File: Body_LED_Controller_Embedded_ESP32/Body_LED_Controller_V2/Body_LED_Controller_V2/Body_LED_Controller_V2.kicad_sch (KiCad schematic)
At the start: 94 parts, among them J1 SERIAL, J10 USB_B_Micro, J11 USB_B_Micro, J12 UnSW_BATT_IN, J13 Conn_02x03_Odd_Even, J14 DomeControllerUSB, J15 DomePlateControllerUSB, J16 UnSW_BATT_PASS, J17 RADH_POW, J18 RASP_POW, J19 5V_OUT_3, J2 I2C, J20 ICSP, J21 DomeElectronicsPowerIn, J22 DB25_Female_MountingHoles, J23 Amplifier_POW, J3 Conn_02x10_Odd_Even, J4 LDP/MAINT, J5 COIN/VU, J6 Batt Level LEDS, J7 Data Panel/ CBI, J8 Spectrum Analyzer, J9 Ext Mic, SW1 SW_Push, SW2 SW_Push, U1 ATMEGA256016AU, U14 D36V50F5-STEPDOWN, U2 CH340C, U3 CJ2301_S1, U4 ESP32-WROOM-32U_16MB_, U5 CH340C, U6 UMH3N, U7 ME6211C33M5G, U8 CJ2301_S1, Y1 16MHz

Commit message: Added a lot since last check in
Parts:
- removed D1, D2: SMD-LED-CLEAR-BLUE(0402), Custom:LED-0402, symbol Custom:SMD-LED-CLEAR-BLUE(0402)
- removed J1: SERIAL, Connector_PinHeader_2.54mm:PinHeader_2x04_P2.54mm_Vertical, symbol Connector_Generic:Conn_02x04_Odd_Even
- removed J13: Conn_02x03_Odd_Even, Connector_PinHeader_2.54mm:PinHeader_2x03_P2.54mm_Vertical, symbol Connector_Generic:Conn_02x03_Odd_Even
- removed J2: I2C, Connector_PinHeader_2.54mm:PinHeader_2x04_P2.54mm_Vertical, symbol Connector_Generic:Conn_02x04_Odd_Even
- removed J4: LDP/MAINT, Connector_PinHeader_2.54mm:PinHeader_2x04_P2.54mm_Vertical, symbol Connector_Generic:Conn_02x04_Odd_Even
- removed J5: COIN/VU, Connector_PinHeader_2.54mm:PinHeader_2x06_P2.54mm_Vertical, symbol Connector_Generic:Conn_02x06_Odd_Even
- removed J9: Ext Mic, Connector_PinHeader_2.54mm:PinHeader_1x03_P2.54mm_Vertical, symbol Connector_Generic:Conn_01x03
- removed R15, R16: 1K, Resistor_SMD:R_0402_1005Metric, symbol Device:R
- removed R4, R5: 10K, Resistor_SMD:R_0402_1005Metric, symbol Device:R
- added J1, J2: Body Servos, Connector_Molex:Molex_KK-254_AE-6410-03A_1x03_P2.54mm_Vertical, symbol Connector_Generic:Conn_01x03
- added J13: Batt Level LEDS, Connector_Molex:Molex_KK-254_AE-6410-04A_1x04_P2.54mm_Vertical, symbol Connector_Generic:Conn_01x04
- added J24: Future, Connector_Molex:Molex_KK-254_AE-6410-03A_1x03_P2.54mm_Vertical, symbol Connector_Generic:Conn_01x03
- added J25: Stealth, Connector_Molex:Molex_KK-254_AE-6410-03A_1x03_P2.54mm_Vertical, symbol Connector_Generic:Conn_01x03
- added J26: RADH, Connector_Molex:Molex_KK-254_AE-6410-03A_1x03_P2.54mm_Vertical, symbol Connector_Generic:Conn_01x03
- added J27: VU Data Panel, Connector_Molex:Molex_KK-254_AE-6410-06A_1x06_P2.54mm_Vertical, symbol Connector_Generic:Conn_01x06
- added J4: LDP, Connector_Molex:Molex_KK-254_AE-6410-04A_1x04_P2.54mm_Vertical, symbol Connector_Generic:Conn_01x04
- added J5: Coin Slots, Connector_Molex:Molex_KK-254_AE-6410-06A_1x06_P2.54mm_Vertical, symbol Connector_Generic:Conn_01x06
- added J9: Maintenance, Connector_Molex:Molex_KK-254_AE-6410-04A_1x04_P2.54mm_Vertical, symbol Connector_Generic:Conn_01x04
- J6: footprint Connector_PinHeader_2.54mm:PinHeader_1x04_P2.54mm_Vertical -> Connector_Molex:Molex_KK-254_AE-6410-04A_1x04_P2.54mm_Vertical
- J7: footprint Connector_PinHeader_2.54mm:PinHeader_1x05_P2.54mm_Vertical -> Connector_Molex:Molex_KK-254_AE-6410-05A_1x05_P2.54mm_Vertical
- J8: footprint Connector_PinHeader_2.54mm:PinHeader_1x06_P2.54mm_Vertical -> Connector_Molex:Molex_KK-254_AE-6410-06A_1x06_P2.54mm_Vertical
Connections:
- net +3.3V_BC: no longer L2.4 (VDD)
- net +5V: now also L2.4 (VDD), J1.2 (Pin_2), J13.2 (Pin_2), J27.2 (Pin_2), J4.2 (Pin_2), J5.2 (Pin_2), J9.2 (Pin_2)
- net CS1_CLOCK: now also J5.3 (Pin_3)
- net CS2_CLOCK: now also J5.5 (Pin_5)
- net EXT_MIC: now also J1.3 (Pin_3)
- net GND: now also J1.1 (Pin_1), J13.1 (Pin_1), J2.1 (Pin_1), J24.1 (Pin_1), J25.1 (Pin_1), J26.1 (Pin_1), J27.1 (Pin_1), J4.1 (Pin_1), J5.1 (Pin_1), J9.1 (Pin_1)
- net LDP_CLOCK: now also J4.3 (Pin_3)
- net MAINT_CLOCK: now also J9.3 (Pin_3)
- net RXD0_BC: now also U4.34 (RXD0)
- net RX_BL: now also U4.23 (IO15); no longer U4.11 (IO26)
- net RX_BS: now also U4.16 (IO13), J2.2 (Pin_2); no longer U4.27 (IO16)
- net RX_MP: now also U4.8 (IO32), J13.3 (Pin_3); no longer U4.28 (IO17)
- net RX_ST: now also U4.7 (IO35), J25.2 (Pin_2); no longer U4.14 (IO12)
- net ST_LED_D_BC: now also U4.29 (IO5); no longer U4.30 (IO18)
- net TX_BL: now also U4.27 (IO16); no longer U4.10 (IO25)
- net TX_BS: now also U4.13 (IO14), J2.3 (Pin_3); no longer U4.23 (IO15)
- net TX_MP: now also U4.30 (IO18), J13.4 (Pin_4); no longer U4.29 (IO5)
- net TX_ST: now also U4.31 (IO19), J25.3 (Pin_3); no longer U4.13 (IO14)
- net VU1_CLOCK: now also J27.3 (Pin_3)
- net VU2_CLOCK: now also J27.5 (Pin_5)
- net at R9.1: now also J5.6 (Pin_6)
- net at R8.1: now also J5.4 (Pin_4)
- net RX_RD: now reaches U4.6 (IO34)
- net RX_RD: now also J26.2 (Pin_2)
- net at R11.2: now also J27.6 (Pin_6)
- net at R10.2: now also J27.4 (Pin_4)
- net at R6.1: now also J4.4 (Pin_4)
- net at R7.2: now also J9.4 (Pin_4)
- net RX1: no longer names the net of U1.45 (PD2)
- net RX3: no longer names the net of U1.63 (PJ0)
- net SCL: no longer names the net of U1.43 (PD0)
- net SDA: no longer names the net of U1.44 (PD1)
- net TX1: no longer names the net of U1.46 (PD3)
- net TX3: no longer names the net of U1.64 (PJ1)
- new net RX_FU: J24.2 (Pin_2), U4.10 (IO25)
- new net TX_FU: J24.3 (Pin_3), U4.11 (IO26)
- new net TX_RD: J26.3 (Pin_3), U4.28 (IO17)
- no-connect marks 86 -> 93
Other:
- note removed: "TX/RX LEDs"
- moved on the sheet: L2, R10, R11, R20, R27, R6, R7, R8, R9, SW2

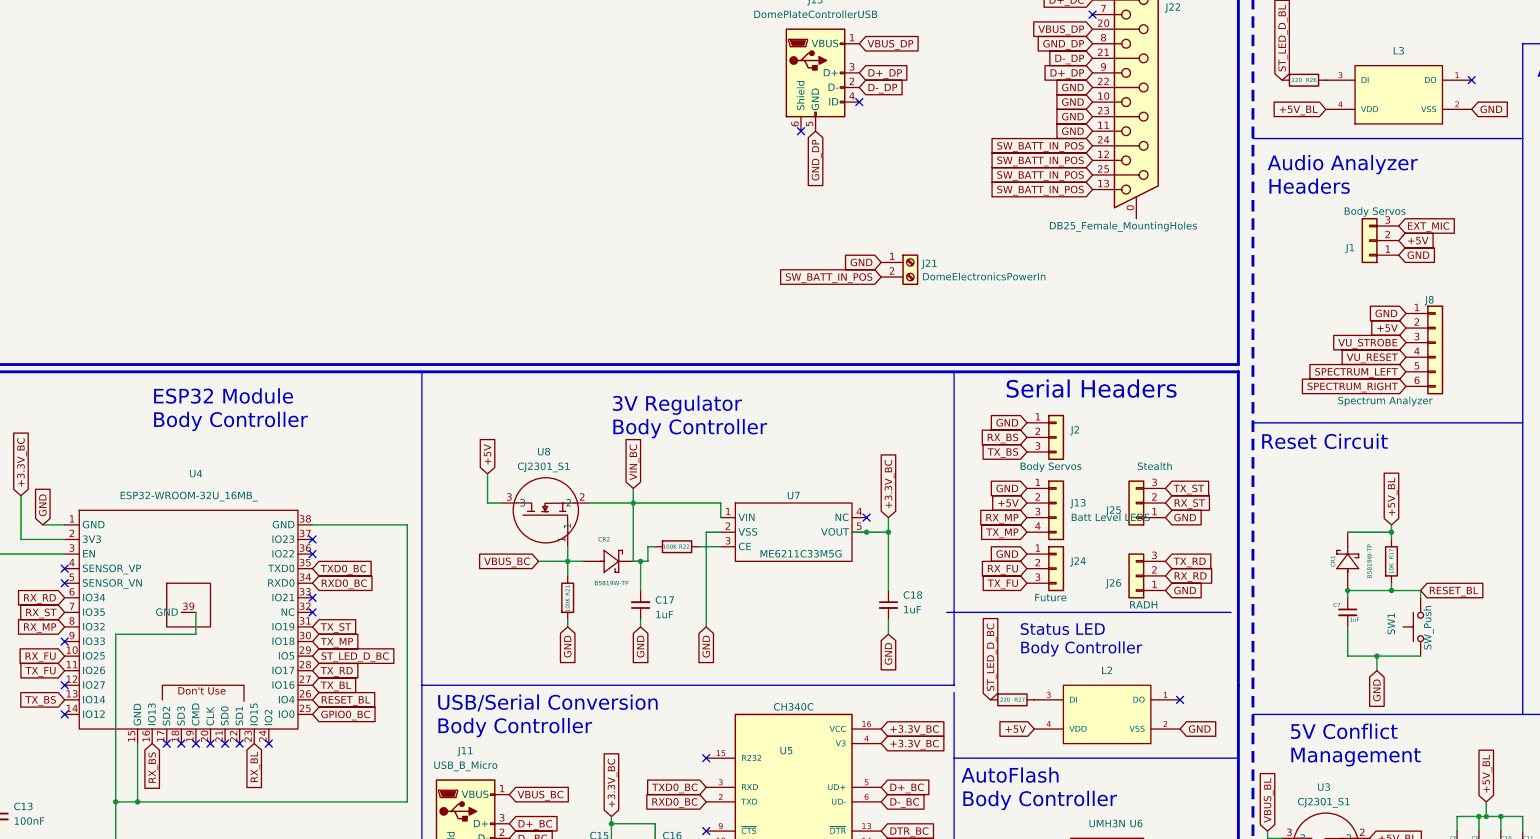
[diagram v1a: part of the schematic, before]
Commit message: added LED PCBs
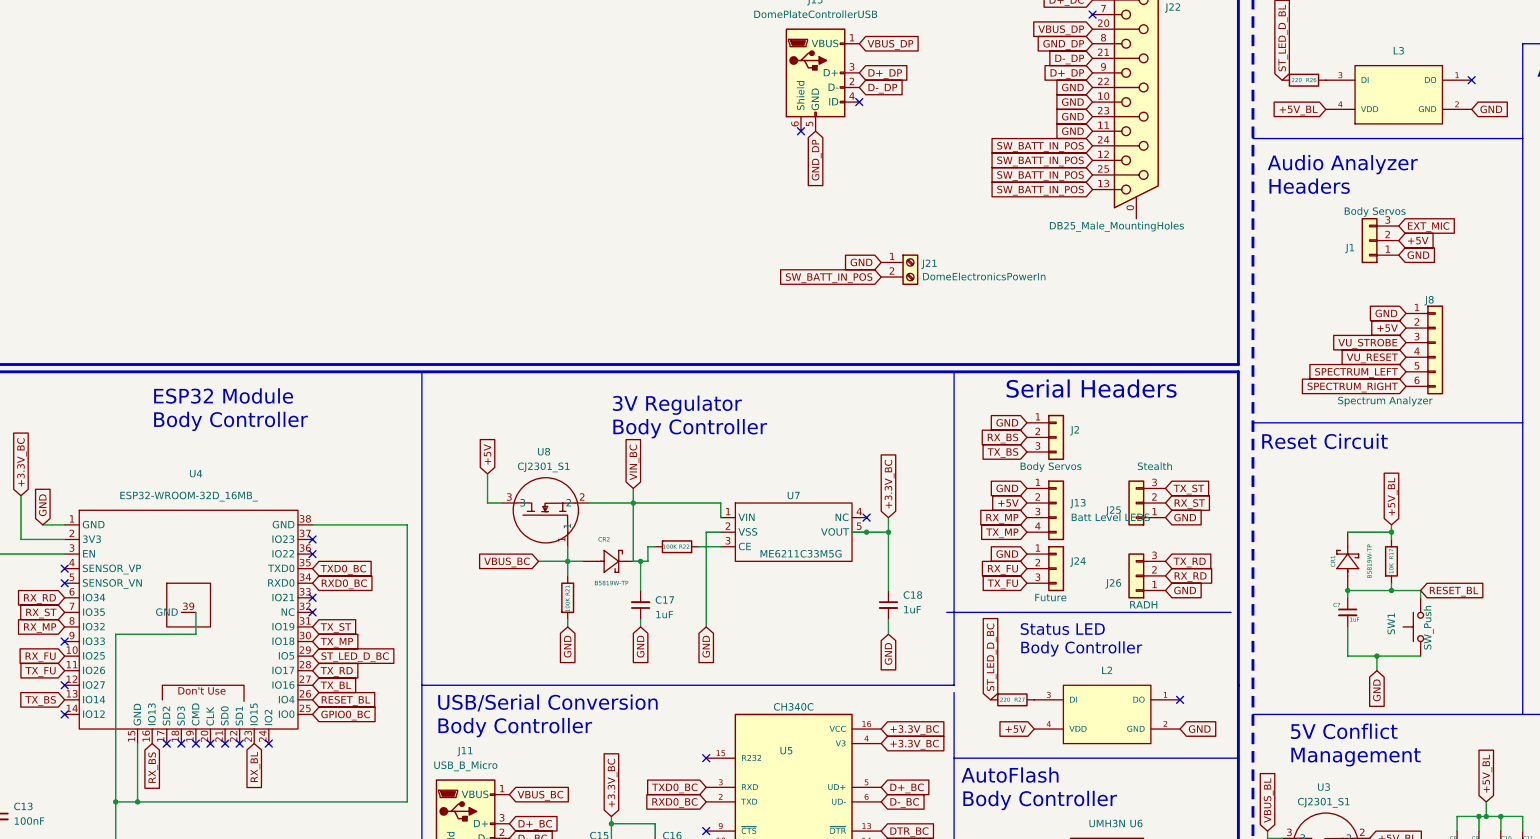
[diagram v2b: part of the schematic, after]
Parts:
- CR2: LCSC (none) -> C84354
- J1, J2, J24, J25, J26: LCSC C20547 -> C471416
- J13, J4, J6, J9: LCSC C390680 -> C240840
- J22: value DB25_Female_MountingHoles -> DB25_Male_MountingHoles; footprint Connector_Dsub:DSUB-25_Female_Vertical_P2.77x2.84mm_MountingHoles -> Connector_Dsub:DSUB-25_Male_Vertical_P2.77x2.84mm_MountingHoles; LCSC (none) -> C2984302
- J27, J5, J8: LCSC C190819 -> C587046
- J7: LCSC C390682 -> C588986
- L2, L3: footprint Custom:WS2812B-2020 -> WS2812B-2020
- R20: LCSC C190321 -> C269701
- R27: LCSC (none) -> C352454
- U2, U5: LCSC C82942 -> C84681
- U4: value ESP32-WROOM-32U_16MB_ -> ESP32-WROOM-32D_16MB_; LCSC C529580 -> C529578
